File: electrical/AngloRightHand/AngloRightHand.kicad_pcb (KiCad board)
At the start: 2 copper layers, 50 parts, among them J4 TC2030-NL, U1 DRV5053VAQDBZR, U10 DRV5053VAQDBZR, U11 DRV5053VAQDBZR, U12 DRV5053VAQDBZR, U13 DRV5053VAQDBZR, U14 DRV5053VAQDBZR, U15 DRV5053VAQDBZR, U16 DRV5053VAQDBZR, U17 DRV5053VAQDBZR, U18 DRV5053VAQDBZR, U19 STM32L072CBTx, U2 CD74HC4067SM, U5 DRV5053VAQDBZR, U6 DRV5053VAQDBZR, U7 DRV5053VAQDBZR, U8 DRV5053VAQDBZR, U9 DRV5053VAQDBZR

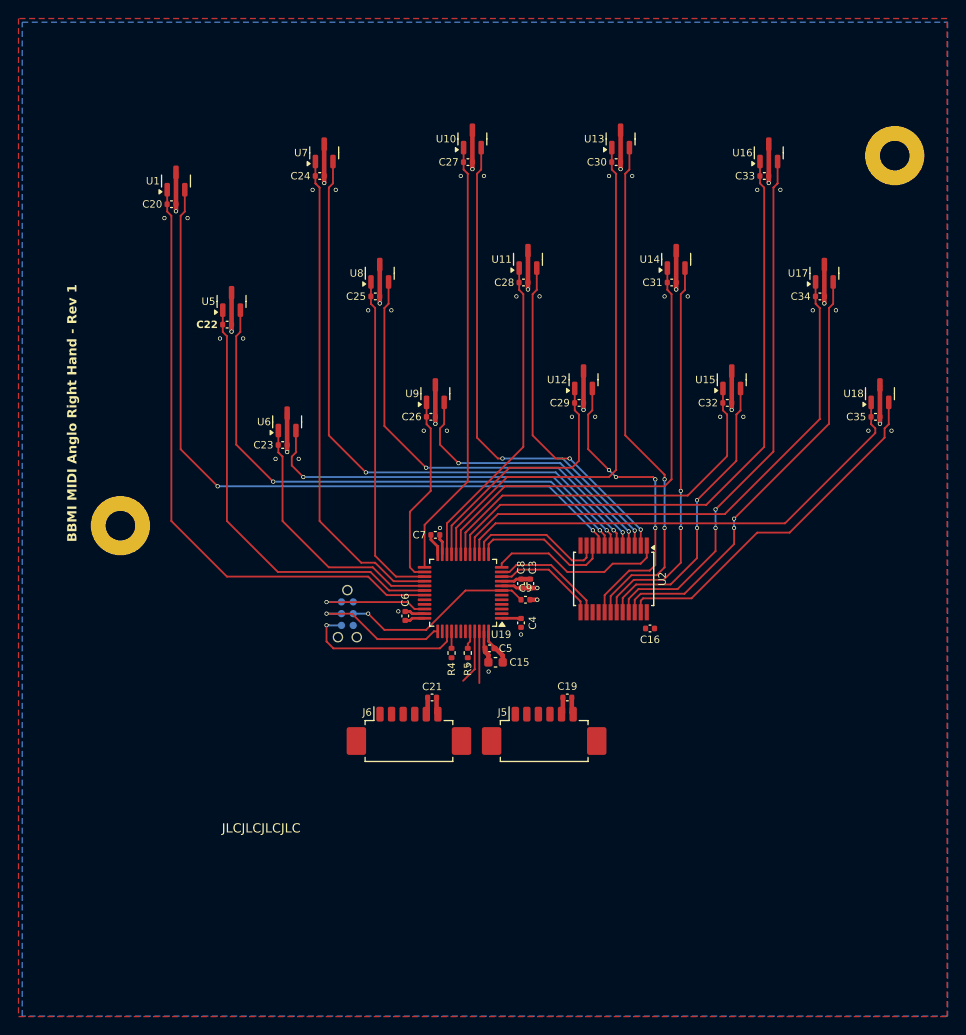
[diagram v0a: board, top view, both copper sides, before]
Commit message: All nets routed for right hand board
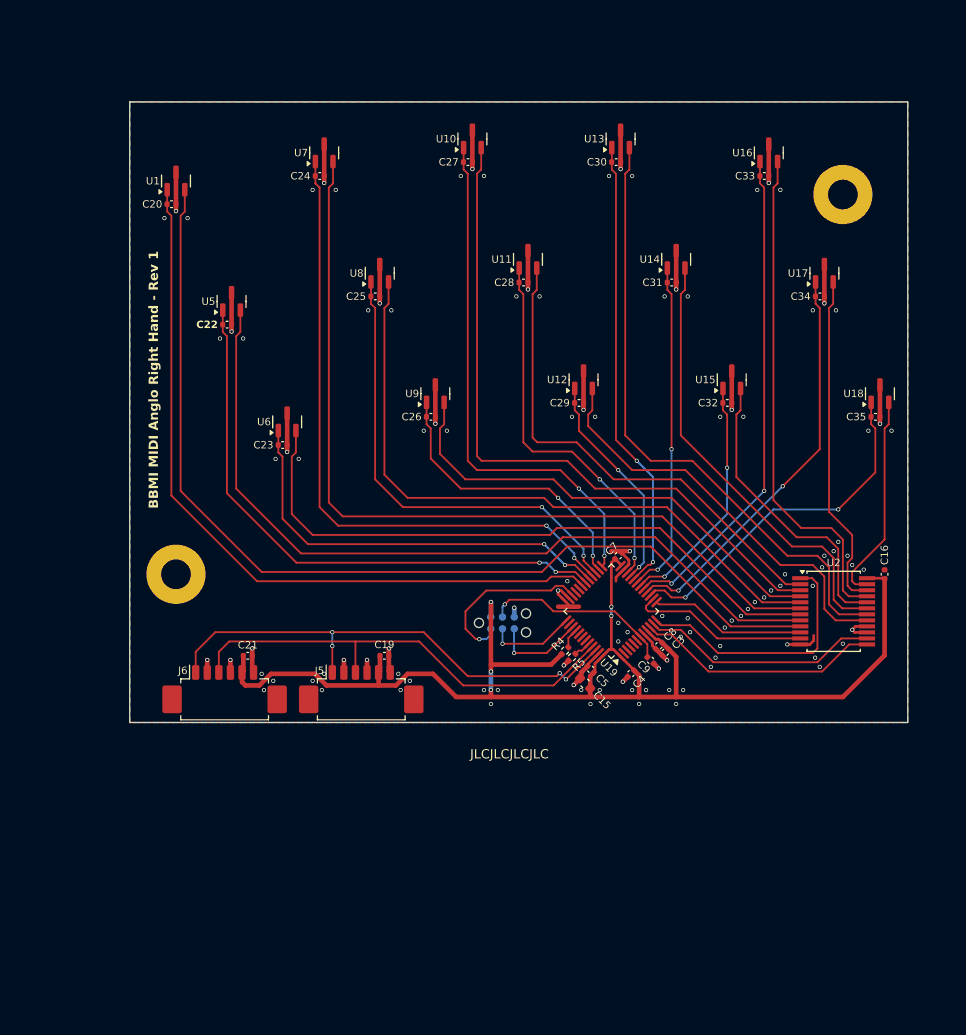
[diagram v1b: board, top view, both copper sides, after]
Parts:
- removed C6: 100nF, Capacitor_SMD:C_0402_1005Metric
- moved C16 26.0 mm to (118.5, 154.0), turned to 90 degrees
- moved U2 24.0 mm to (113.0, 158.0), turned to 0 degrees
- moved C21 20.4 mm to (49.8, 162.8)
- moved J6 20.4 mm to (47.2, 167.0)
- moved C19 20.3 mm to (64.5, 162.8)
- moved J5 20.3 mm to (62.0, 167.0)
- moved C7 19.9 mm to (89.8, 152.0), turned to 45 degrees
- moved J4 16.8 mm to (77.2, 159.2), turned to 0 degrees
- moved C3 16.4 mm to (94.8, 162.4), turned to -135 degrees
- moved C8 16.3 mm to (94.1, 161.7), turned to -135 degrees
- moved U19 16.1 mm to (89.0, 158.0), turned to 135 degrees
- moved C9 15.0 mm to (93.2, 163.3), turned to -45 degrees
- moved C4 13.1 mm to (91.1, 164.7), turned to -135 degrees
- moved R4 12.3 mm to (84.0, 162.2), turned to 45 degrees
- moved R5 11.3 mm to (84.8, 162.9), turned to -135 degrees
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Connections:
- U19 pad 36: +3.3V -> GND
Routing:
- net +3.3V: track 17.6 -> 142.6 mm, vias 0 -> 5
- net I2C_SDA: track 5.59 -> 54.3 mm, vias 0 -> 4
- net I2C_SCL: track 5.86 -> 50.1 mm
- net BUTTON_1a: track 78.2 -> 107.9 mm, vias 2 -> 0
- net BUTTON_1: track 59.7 -> 87.7 mm, vias 2 -> 0
- net BUTTON_6: track 42.7 -> 69.2 mm, vias 2 -> 0
- net BUTTON_2a: track 66.5 -> 92.6 mm, vias 2 -> 0
- net GND: track 79.2 -> 103.8 mm, vias 52 -> 113
- net BUTTON_2: track 47.7 -> 71.6 mm, vias 2 -> 0
- net BUTTON_7: track 30.5 -> 51.0 mm, vias 2 -> 0
- net BUTTON_3a: track 54.3 -> 74.4 mm, vias 2 -> 0
- net BUTTON_3: track 35.9 -> 54.0 mm, vias 2 -> 0
- net BUTTON_EN_6: track 28.2 -> 45.5 mm, vias 0 -> 2
- net BUTTON_EN_2a: track 53.0 -> 70.3 mm, vias 0 -> 2
- net BUTTON_10: track 38.9 -> 22.7 mm
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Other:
- board outline added: 84 x 67 mm

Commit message: Reduce size of right hand board
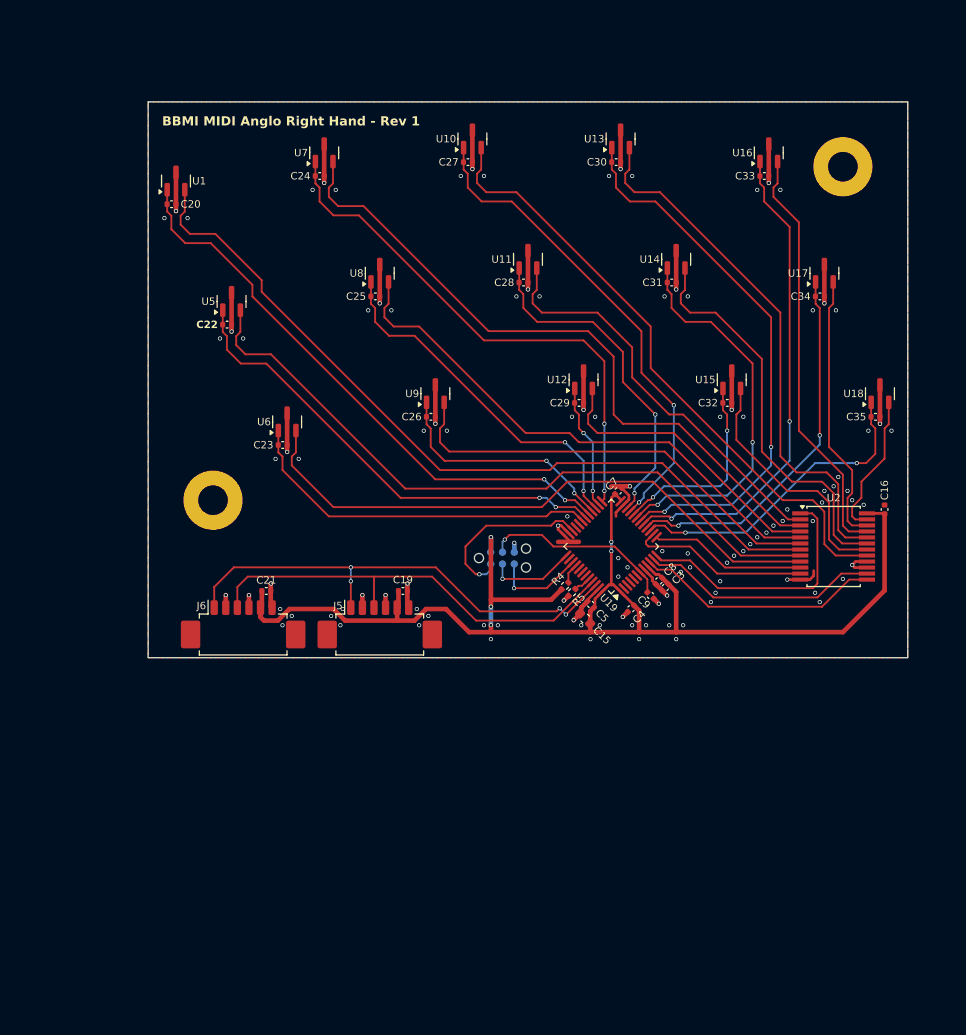
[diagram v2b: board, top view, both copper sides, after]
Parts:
- moved H2 8.94 mm to (46.0, 146.0)
- moved C19 7.28 mm to (66.5, 155.8)
- moved C21 7.28 mm to (51.8, 155.8)
- moved J5 7.28 mm to (64.0, 160.0)
- moved J6 7.28 mm to (49.2, 160.0)
- moved C15 7.00 mm to (86.2, 158.8)
- moved C16 7.00 mm to (118.5, 147.0)
- moved C3 7.00 mm to (94.8, 155.4)
- moved C4 7.00 mm to (91.1, 157.7)
- moved C5 7.00 mm to (86.8, 157.3)
- moved C7 7.00 mm to (89.8, 145.0)
- moved C8 7.00 mm to (94.1, 154.7)
- moved C9 7.00 mm to (93.2, 156.3)
- moved J4 7.00 mm to (77.2, 152.2)
- moved R4 7.00 mm to (84.0, 155.2)
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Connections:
- U19 pad 18: BUTTON_EN_9 -> BUTTON_EN_4a
- U19 pad 20: BUTTON_EN_4a -> BUTTON_EN_9
- U19 pad 21: BUTTON_EN_8 -> BUTTON_EN_3a
- U19 pad 25: BUTTON_EN_3a -> BUTTON_EN_2a
- U19 pad 26: BUTTON_EN_7 -> BUTTON_EN_8
- U19 pad 28: BUTTON_EN_2a -> BUTTON_EN_7
- U19 pad 29: BUTTON_EN_6 -> BUTTON_EN_1a
- U19 pad 31: BUTTON_EN_1a -> BUTTON_EN_6
- U2 pad 17: BUTTON_8 -> BUTTON_3a
- U2 pad 18: BUTTON_4a -> BUTTON_9
- U2 pad 20: BUTTON_9 -> BUTTON_4a
- U2 pad 3: BUTTON_3a -> BUTTON_2a
- U2 pad 4: BUTTON_7 -> BUTTON_8
- U2 pad 6: BUTTON_2a -> BUTTON_7
- U2 pad 7: BUTTON_6 -> BUTTON_1a
- U2 pad 9: BUTTON_1a -> BUTTON_6
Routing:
- net BUTTON_1a: track 107.9 -> 86.7 mm
- net BUTTON_2a: track 92.6 -> 73.3 mm
- net BUTTON_EN_1a: track 82.0 -> 63.0 mm, vias 0 -> 2
- net BUTTON_8: track 45.1 -> 31.7 mm
- net BUTTON_2: track 71.6 -> 58.7 mm
- net BUTTON_EN_2a: track 70.3 -> 57.6 mm
- net BUTTON_EN_1: track 62.7 -> 50.7 mm
- net BUTTON_1: track 87.7 -> 75.7 mm
- net BUTTON_EN_2: track 50.2 -> 38.8 mm
- net BUTTON_EN_8: track 23.9 -> 13.6 mm
- net BUTTON_EN_4a: track 49.4 -> 59.7 mm
- net BUTTON_4a: track 67.7 -> 58.0 mm
- net BUTTON_3: track 54.0 -> 44.5 mm
- net BUTTON_5a: track 54.4 -> 45.5 mm
- net BUTTON_10: track 22.7 -> 15.7 mm
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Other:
- board size 84 x 67 mm -> 82 x 60 mm
- board text removed: "JLCJLCJLCJLC"

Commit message: Clean up right hand schematic
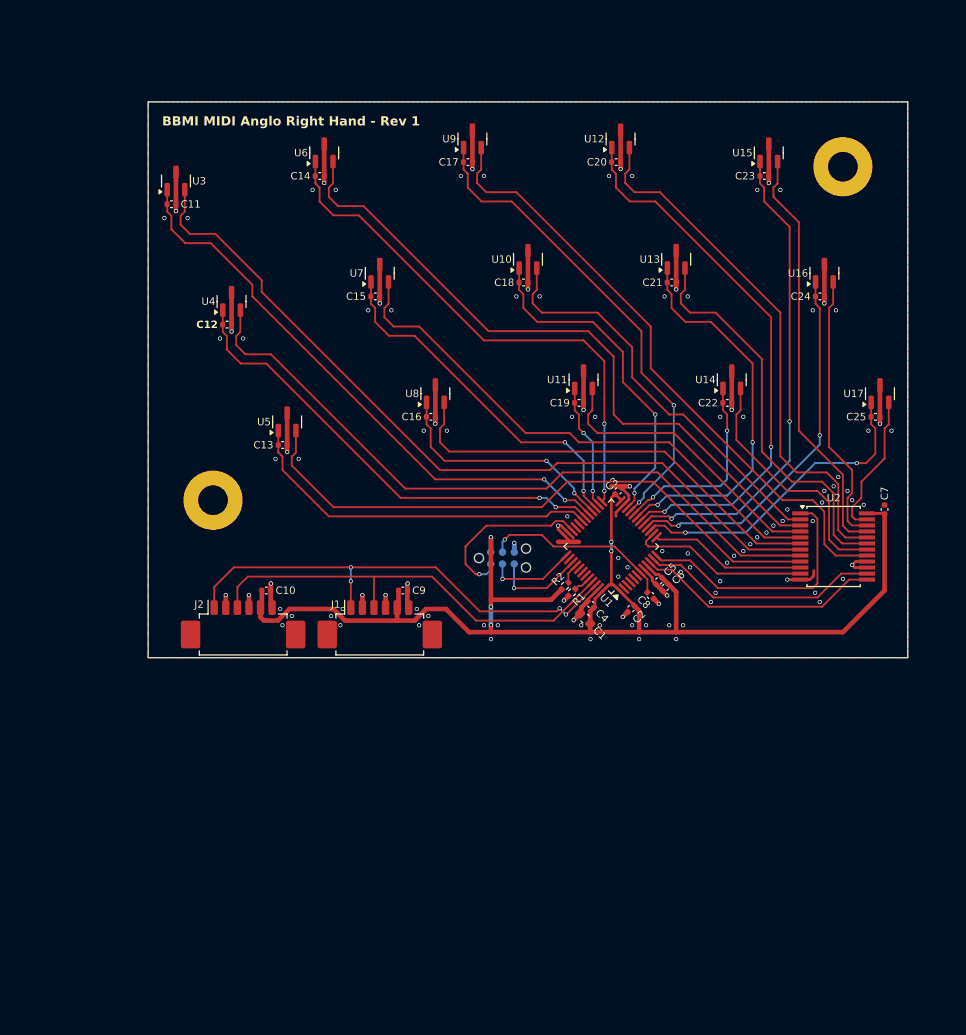
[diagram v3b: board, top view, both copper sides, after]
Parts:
- moved C10 0.05 mm to (51.8, 155.8)
- moved C9 0.05 mm to (66.5, 155.8)
- renumbered C15 to C1, C21 to C10, C20 to C11, C22 to C12, C23 to C13, C24 to C14, C25 to C15, C26 to C16, C27 to C17, C28 to C18, C29 to C19, C4 to C2, C30 to C20, C31 to C21, C32 to C22, C33 to C23, C34 to C24, C35 to C25, C7 to C3, C5 to C4, C8 to C5, C3 to C6, C16 to C7, C9 to C8, C19 to C9, J5 to J1, J6 to J2, J4 to J3, R5 to R1, R4 to R2, U19 to U1, U11 to U10, U12 to U11, U13 to U12, U14 to U13, U15 to U14, U16 to U15, U17 to U16, U18 to U17, U1 to U3, U5 to U4, U6 to U5, U7 to U6, U8 to U7, U9 to U8, U10 to U9

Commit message: Renumber parts on right hand board
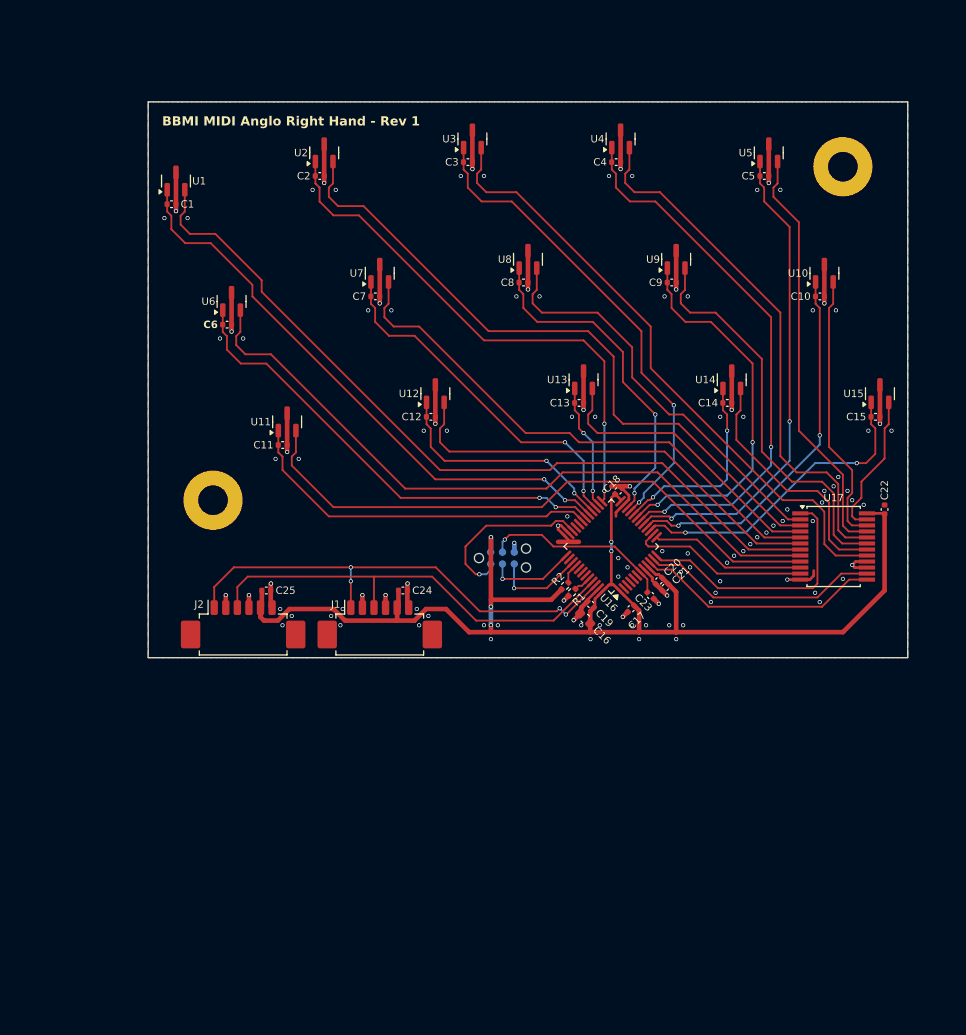
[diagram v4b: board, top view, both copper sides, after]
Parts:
- renumbered C11 to C1, C24 to C10, C13 to C11, C16 to C12, C19 to C13, C22 to C14, C25 to C15, C1 to C16, C2 to C17, C3 to C18, C4 to C19, C14 to C2, C5 to C20, C6 to C21, C7 to C22, C8 to C23, C9 to C24, C10 to C25, C17 to C3, C20 to C4, C23 to C5, C12 to C6, C15 to C7, C18 to C8, C21 to C9, U3 to U1, U16 to U10, U5 to U11, U8 to U12, U11 to U13, U17 to U15, U1 to U16, U2 to U17, U6 to U2, U9 to U3, U12 to U4, U15 to U5, U4 to U6, U10 to U8, U13 to U9

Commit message: Change board label silkscreen
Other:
- board text added: "MIDI Anglo Right Hand - Rev 1"
- board text removed: "BBMI MIDI Anglo Right Hand - Rev 1"
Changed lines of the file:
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@@
 		(layer "Edge.Cuts")
 	)
-	(gr_text "BBMI MIDI Anglo Right Hand - Rev 1"
+	(gr_text "MIDI Anglo Right Hand - Rev 1"
 		(at 40.5 104.5 0)
 		(layer "F.SilkS")

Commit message: Add stitching vias
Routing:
- net BUTTON_5a: track 45.5 -> 46.9 mm
- net GND: track 103.8 -> 103.7 mm, vias 113 -> 517

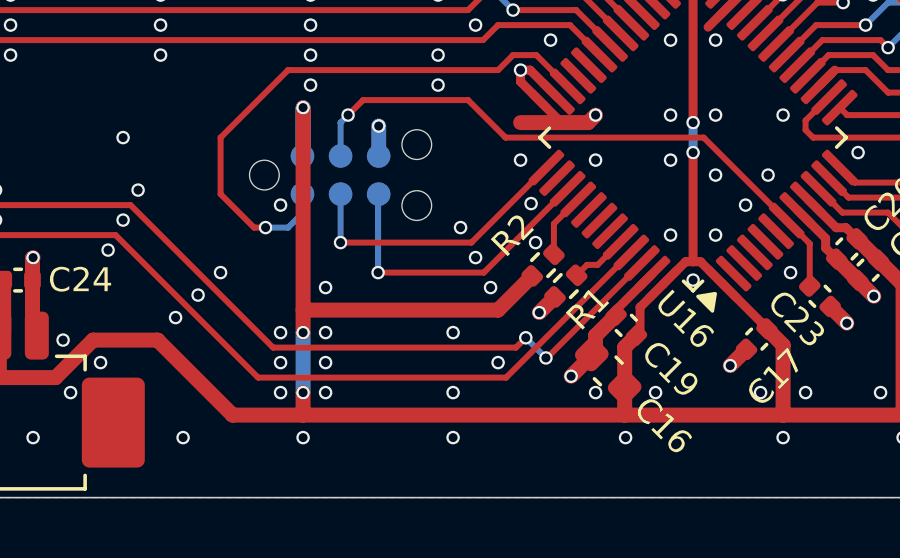
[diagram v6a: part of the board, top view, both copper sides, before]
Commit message: Swap SDA and SCL on button board connectors
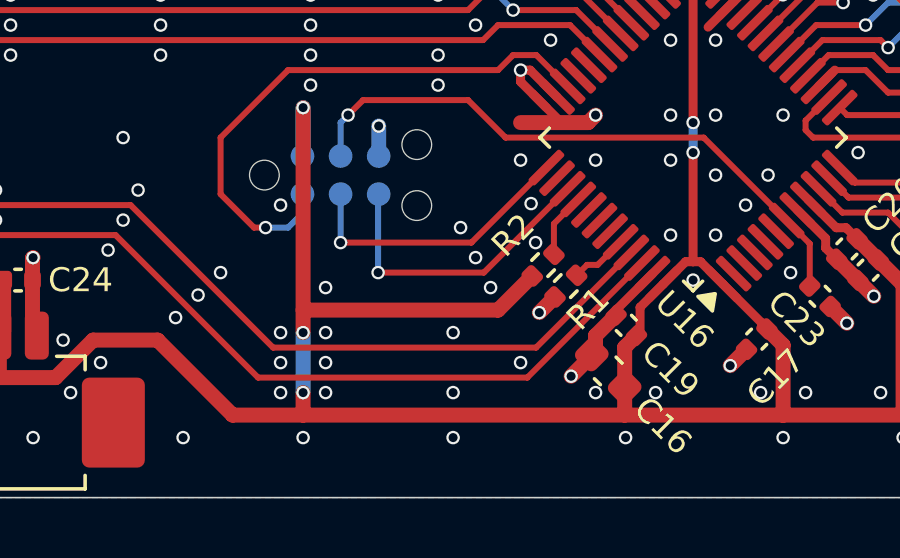
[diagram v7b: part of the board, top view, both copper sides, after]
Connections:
- J1 pad 1: I2C_SDA -> I2C_SCL
- J1 pad 3: I2C_SCL -> I2C_SDA
- J2 pad 1: I2C_SDA -> I2C_SCL
- J2 pad 3: I2C_SCL -> I2C_SDA
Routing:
- net I2C_SDA: track 52.3 -> 48.3 mm, vias 4 -> 0
- net I2C_SCL: track 48.1 -> 51.6 mm, vias 0 -> 2
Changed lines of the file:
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@@
 			(layers "F.Cu" "F.Mask" "F.Paste")
 			(roundrect_rratio 0.25)
-			(net 15 "I2C_SDA")
+			(net 14 "I2C_SCL")
 			(pinfunction "Pin_1")
 			(pintype "passive")
@@
 			(layers "F.Cu" "F.Mask" "F.Paste")
 			(roundrect_rratio 0.25)
-			(net 14 "I2C_SCL")
+			(net 15 "I2C_SDA")
 			(pinfunction "Pin_3")
 			(pintype "passive")
@@
 			(layers "F.Cu" "F.Mask" "F.Paste")
 			(roundrect_rratio 0.25)
-			(net 15 "I2C_SDA")
+			(net 14 "I2C_SCL")
 			(pinfunction "Pin_1")
 			(pintype "passive")
@@
 			(layers "F.Cu" "F.Mask" "F.Paste")
 			(roundrect_rratio 0.25)
-			(net 14 "I2C_SCL")
+			(net 15 "I2C_SDA")
 			(pinfunction "Pin_3")
 			(pintype "passive")
@@
 	)
 	(via
-		(at 82.5 158.5)
+		(at 83.25 158.5)
 		(size 0.45)
 		(drill 0.3)
@@
 	)
 	(segment
-		(start 48.625 155.375)
-		(end 49.75 154.25)
+		(start 83.767766 158)
+		(end 75 158)
 		(width 0.2)
 		(layer "F.Cu")
@@
 	)
 	(segment
-		(start 74.5 159)
-		(end 82.767767 159)
+		(start 48.25 153.25)
+		(end 46.125 155.375)
 		(width 0.2)
 		(layer "F.Cu")
@@
 	)
 	(segment
-		(start 48.625 157.6)
-		(end 48.625 155.375)
+		(start 60.875 154.75)
+		(end 60.875 157.6)
 		(width 0.2)
 		(layer "F.Cu")
@@
 	)
 	(segment
-		(start 82.767767 159)
-		(end 86.940552 154.827215)
+		(start 60.875 153.25)
+		(end 48.25 153.25)
 		(width 0.2)
 		(layer "F.Cu")
@@
 	)
 	(segment
-		(start 63.375 157.6)
-		(end 63.375 154.25)
+		(start 75 158)
+		(end 70.25 153.25)
 		(width 0.2)
 		(layer "F.Cu")
@@
 	)
 	(segment
-		(start 49.75 154.25)
-		(end 69.75 154.25)
+		(start 46.125 155.375)
+		(end 46.125 157.6)
 		(width 0.2)
 		(layer "F.Cu")
@@
 	)
 	(segment
-		(start 69.75 154.25)
-		(end 74.5 159)
+		(start 86.940551 154.827215)
+		(end 83.767766 158)
 		(width 0.2)
 		(layer "F.Cu")
@@
 	)
 	(segment
-		(start 75 158)
-		(end 70.25 153.25)
+		(start 70.25 153.25)
+		(end 60.875 153.25)
 		(width 0.2)
 		(layer "F.Cu")
-		(net 15)
+		(net 14)
 	)
-	(segment
-		(start 48.25 153.25)
-		(end 46.125 155.375)
-		(width 0.2)
-		(layer "F.Cu")
-		(net 15)
+	(via
+		(at 60.875 153.25)
+		(size 0.45)
+		(drill 0.3)
+		(layers "F.Cu" "B.Cu")
+		(net 14)
+	)
+	(via
+		(at 60.875 154.75)
+		(size 0.45)
+		(drill 0.3)
+		(layers "F.Cu" "B.Cu")
+		(net 14)
 	)
 	(segment
 		(start 60.875 154.75)
-		(end 60.875 157.6)
+		(end 60.875 153.25)
 		(width 0.2)
-		(layer "F.Cu")
-		(net 15)
+		(layer "B.Cu")
+		(net 14)
 	)
 	(segment
-		(start 84.094759 158.34476)
-		(end 84.130113 158.34476)
+		(start 83.474874 159)
+		(end 87.294105 155.180769)
 		(width 0.2)
 		(layer "F.Cu")
@@
 	)
 	(segment
-		(start 60.875 153.25)
-		(end 48.25 153.25)
+		(start 48.625 157.6)
+		(end 48.625 155.375)
 		(width 0.2)
 		(layer "F.Cu")
@@
 	)
 	(segment
-		(start 46.125 155.375)
-		(end 46.125 157.6)
+		(start 49.75 154.25)
+		(end 69.75 154.25)
 		(width 0.2)
 		(layer "F.Cu")
@@
 	)
 	(segment
-		(start 83.423007 157.673007)
-		(end 83.096015 158)
+		(start 74.5 159)
+		(end 83.474874 159)
 		(width 0.2)
 		(layer "F.Cu")
@@
 	)
 	(segment
-		(start 84.130113 158.34476)
-		(end 87.294105 155.180768)
+		(start 63.375 157.6)
+		(end 63.375 154.25)
 		(width 0.2)
 		(layer "F.Cu")
@@
 	)
 	(segment
-		(start 83.096015 158)
-		(end 75 158)
+		(start 69.75 154.25)
+		(end 74.5 159)
 		(width 0.2)
 		(layer "F.Cu")
@@
 	)
 	(segment
-		(start 70.25 153.25)
-		(end 60.875 153.25)
+		(start 48.625 155.375)
+		(end 49.75 154.25)
 		(width 0.2)
 		(layer "F.Cu")
 		(net 15)
 	)
-	(via
-		(at 60.875 153.25)
-		(size 0.45)
-		(drill 0.3)
-		(layers "F.Cu" "B.Cu")
-		(net 15)
-	)
-	(via
-		(at 84.094759 158.34476)
-		(size 0.45)
-		(drill 0.3)
-		(layers "F.Cu" "B.Cu")
-		(net 15)
-	)
-	(via
-		(at 60.875 154.75)
-		(size 0.45)
-		(drill 0.3)
-		(layers "F.Cu" "B.Cu")
-		(net 15)
-	)
-	(via
-		(at 83.423007 157.673007)
-		(size 0.45)
-		(drill 0.3)
-		(layers "F.Cu" "B.Cu")
-		(net 15)
-	)
-	(segment
-		(start 60.875 154.75)
-		(end 60.875 153.25)
-		(width 0.2)
-		(layer "B.Cu")
-		(net 15)
-	)
-	(segment
-		(start 83.423007 157.673008)
-		(end 83.423007 157.673007)
-		(width 0.2)
-		(layer "B.Cu")
-		(net 15)
-	)
-	(segment
-		(start 84.094759 158.34476)
-		(end 83.423007 157.673008)
-		(width 0.2)
-		(layer "B.Cu")
-		(net 15)
-	)

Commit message: PCB adjustments
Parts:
- H1, H2: footprint MountingHole:MountingHole_3.2mm_M3_Pad -> MountingHole:MountingHole_3.2mm_M3
- moved C25 0.25 mm to (51.5, 155.8)
- moved J2 0.25 mm to (49.0, 160.0)
